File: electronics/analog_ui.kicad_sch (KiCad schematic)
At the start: 21 parts, among them J25 Conn_01x08, SW1 SW_Push, SW2 SW_Push, SW3 SW_Push, SW4 SW_Push, SW5 SW_Push

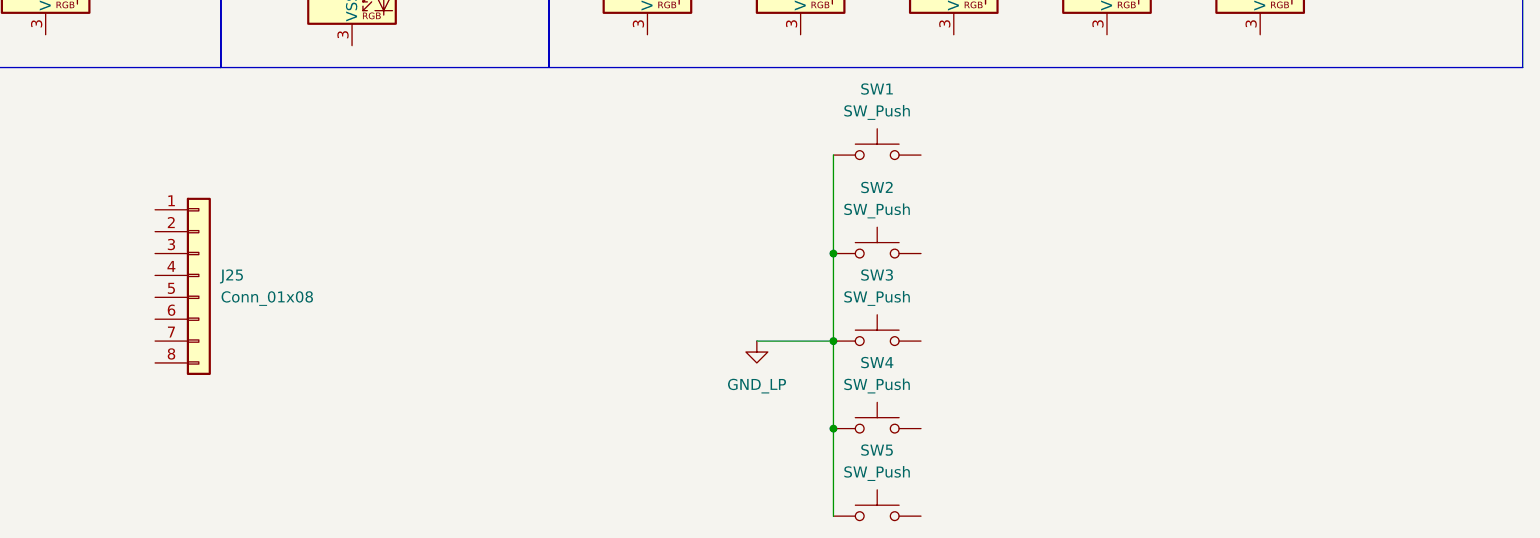
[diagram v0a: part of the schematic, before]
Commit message: basic temp sensor on RMT DS18B20. analogUI stopped working...
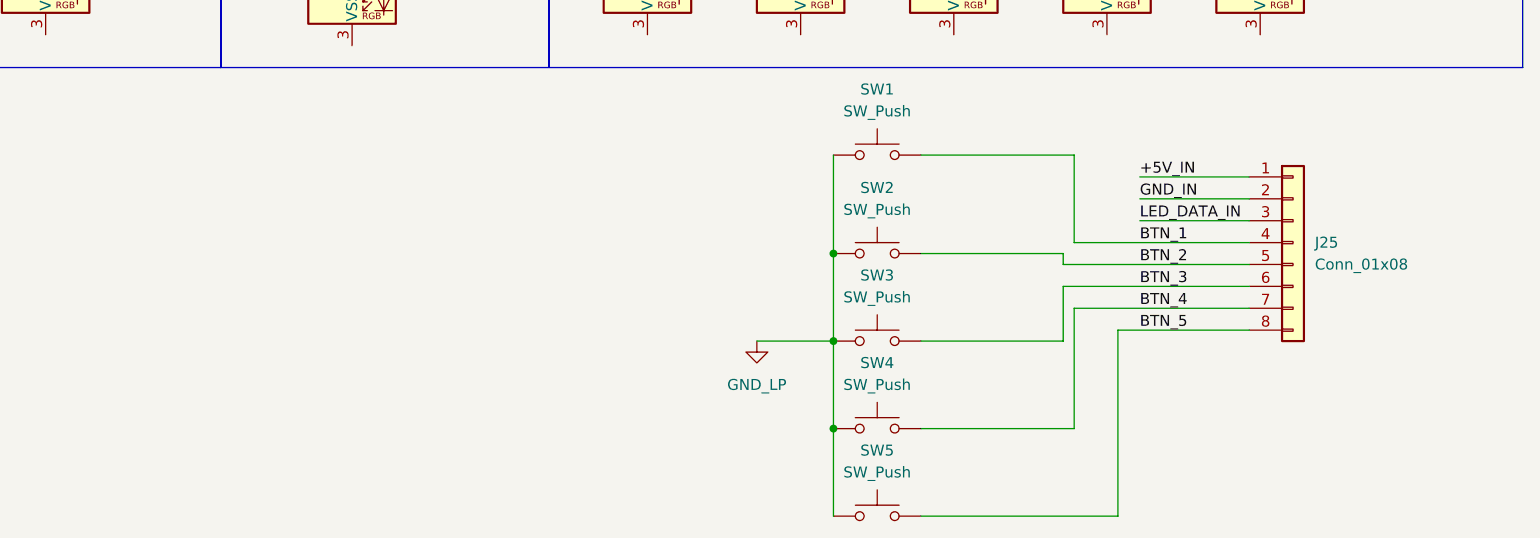
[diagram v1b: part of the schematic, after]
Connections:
- net +5V_IN: now reaches J25.1 (Pin_1)
- net GND_IN: now reaches J25.2 (Pin_2)
- net LED_DATA_IN: now reaches J25.3 (Pin_3)
- net BTN_1: now reaches J25.4 (Pin_4)
- net BTN_1: now also SW1.2
- net BTN_2: now reaches J25.5 (Pin_5)
- net BTN_2: now also SW2.2
- net BTN_3: now reaches J25.6 (Pin_6)
- net BTN_3: now also SW3.2
- net BTN_4: now reaches J25.7 (Pin_7)
- net BTN_4: now also SW4.2
- net BTN_5: now reaches J25.8 (Pin_8)
- net BTN_5: now also SW5.2
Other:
- moved on the sheet: J25

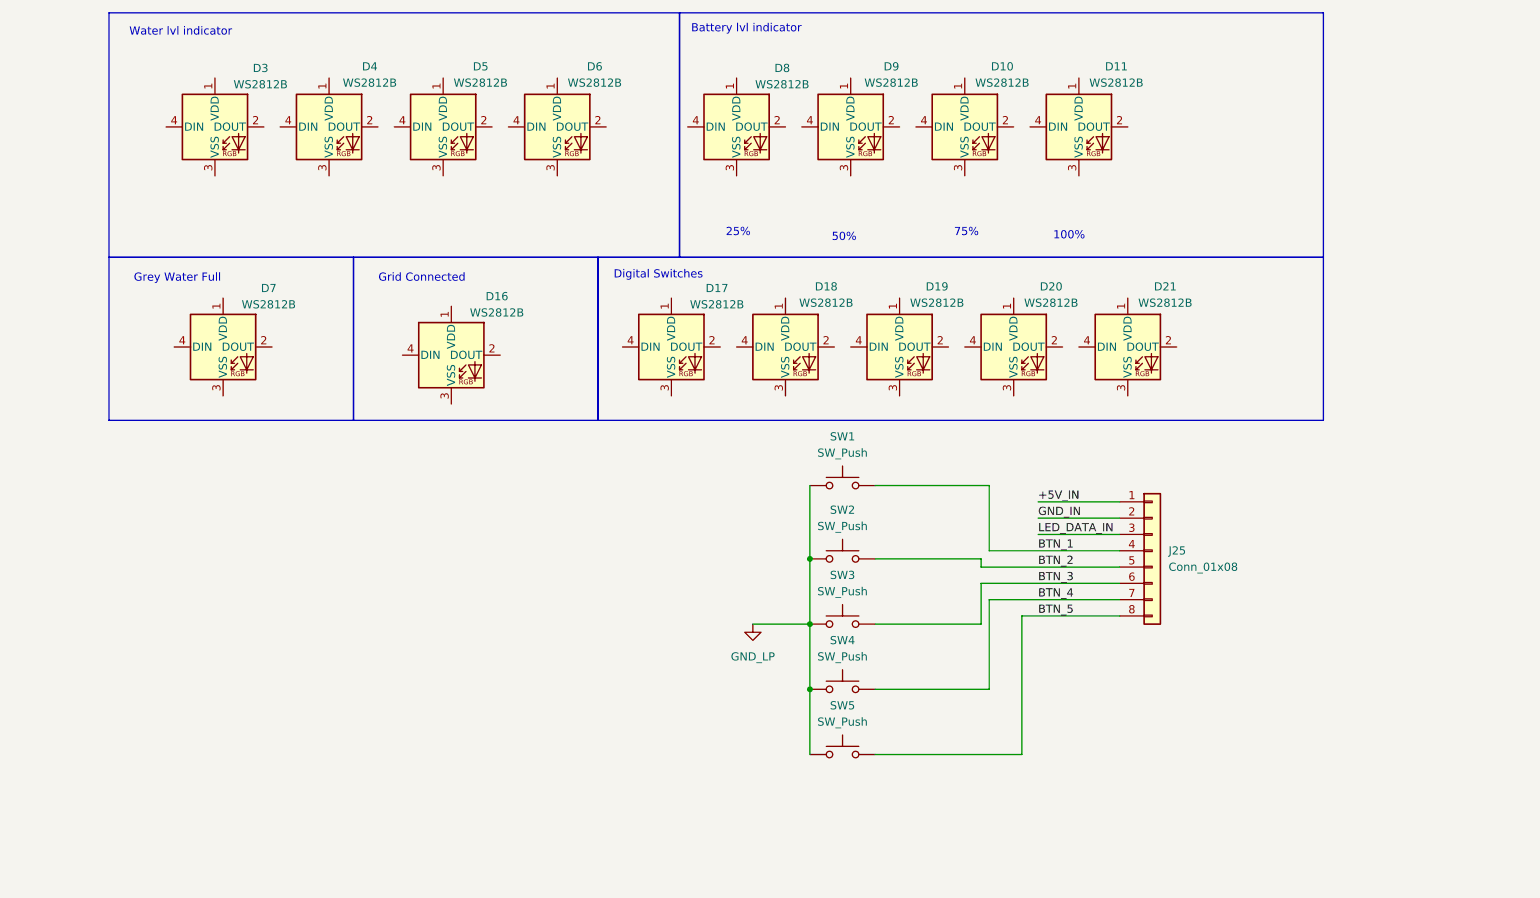
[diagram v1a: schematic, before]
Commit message: start to create BOM and finalising symbol fields
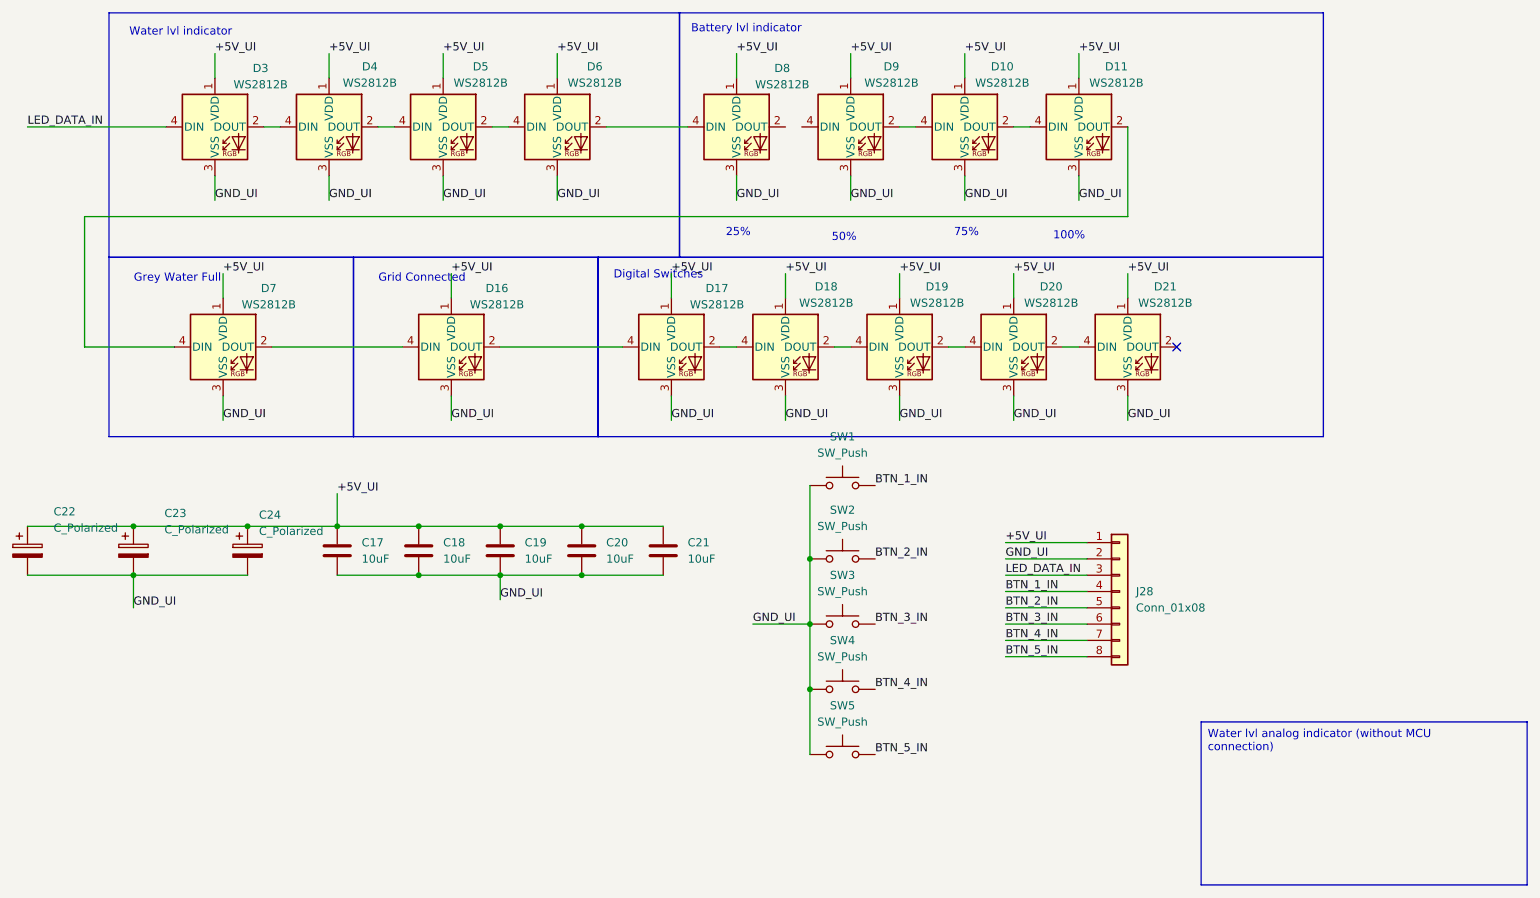
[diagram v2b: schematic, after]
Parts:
- removed J25: Conn_01x08, TerminalBlock:TerminalBlock_Xinya_XY308-2.54-8P_1x08_P2.54mm_Horizontal, symbol Connector_Generic:Conn_01x08
- added C17, C18, C19, C20, C21: 10uF, Capacitor_SMD:C_0805_2012Metric, symbol Device:C
- added C22, C23, C24: C_Polarized, Capacitor_THT:CP_Radial_D5.0mm_P2.50mm, symbol Device:C_Polarized
- added J28: Conn_01x08, TerminalBlock:TerminalBlock_Xinya_XY308-2.54-8P_1x08_P2.54mm_Horizontal, symbol Connector_Generic:Conn_01x08
- D10, D11, D16, D17, D18, D19, D20, D21, D3, D4, D5, D6, D7, D8, D9: footprint LED_SMD:LED_WS2812B-Mini_PLCC4_3.5x3.5mm -> LED_SMD:LED_WS2812B_PLCC4_5.0x5.0mm_P3.2mm
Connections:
- net GND_LP is gone; now on net GND_UI: SW1.1, SW2.1, SW3.1, SW4.1, SW5.1
- net LED_DATA_IN: now also D3.4 (DIN), J28.3 (Pin_3)
- net +5V_UI: now reaches D18.1 (VDD)
- net +5V_UI: now also D10.1 (VDD), D11.1 (VDD), D16.1 (VDD), D17.1 (VDD), D19.1 (VDD), D20.1 (VDD), D21.1 (VDD), D3.1 (VDD), D4.1 (VDD), D5.1 (VDD), D6.1 (VDD), D7.1 (VDD), D8.1 (VDD), D9.1 (VDD), C17.1, C18.1, C19.1, C20.1, C21.1, C22.1, C23.1, C24.1, J28.1 (Pin_1)
- net at D18.2 (DOUT): now also D19.4 (DIN)
- net GND_UI: now reaches D18.3 (VSS)
- net GND_UI: now also D10.3 (VSS), D11.3 (VSS), D16.3 (VSS), D17.3 (VSS), D19.3 (VSS), D20.3 (VSS), D21.3 (VSS), D3.3 (VSS), D4.3 (VSS), D5.3 (VSS), D6.3 (VSS), D7.3 (VSS), D8.3 (VSS), D9.3 (VSS), C17.2, C18.2, C19.2, C20.2, C21.2, C22.2, C23.2, C24.2, J28.2 (Pin_2)
- net at D18.4 (DIN): now also D17.2 (DOUT)
- net at D20.2 (DOUT): now also D21.4 (DIN)
- net at D20.4 (DIN): now also D19.2 (DOUT)
- net at D3.2 (DOUT): now also D4.4 (DIN)
- net at D5.2 (DOUT): now also D6.4 (DIN)
- net at D5.4 (DIN): now also D4.2 (DOUT)
- net at D10.2 (DOUT): now also D11.4 (DIN)
- net at D10.4 (DIN): now also D9.2 (DOUT)
- net at D17.4 (DIN): now also D16.2 (DOUT)
- net at D8.4 (DIN): now also D6.2 (DOUT)
- net at D7.2 (DOUT): now also D16.4 (DIN)
- net at D7.4 (DIN): now also D11.2 (DOUT)
- net BTN_1 renamed BTN_1_IN
- net BTN_1_IN: now also J28.4 (Pin_4)
- net BTN_2 renamed BTN_2_IN
- net BTN_2_IN: now also J28.5 (Pin_5)
- net BTN_3 renamed BTN_3_IN
- net BTN_3_IN: now also J28.6 (Pin_6)
- net BTN_4 renamed BTN_4_IN
- net BTN_4_IN: now also J28.7 (Pin_7)
- net BTN_5 renamed BTN_5_IN
- net BTN_5_IN: now also J28.8 (Pin_8)
- no-connect marks 0 -> 1
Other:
- moved on the sheet: D16
